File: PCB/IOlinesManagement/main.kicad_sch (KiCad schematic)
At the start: 3 parts

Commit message: Fingerprints assignment
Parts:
- DirControl_1, I/O-LinesToDev_1, I/O-LinesToMicro_1: footprint (none) -> Connector_PinHeader_2.54mm:PinHeader_2x09_P2.54mm_Vertical
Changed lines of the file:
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@@
 			)
 		)
-		(property "Footprint" ""
+		(property "Footprint" "Connector_PinHeader_2.54mm:PinHeader_2x09_P2.54mm_Vertical"
 			(at 222.504 69.088 0)
 			(effects
@@
 			)
 		)
-		(property "Footprint" ""
+		(property "Footprint" "Connector_PinHeader_2.54mm:PinHeader_2x09_P2.54mm_Vertical"
 			(at 139.7 68.834 0)
 			(effects
@@
 			)
 		)
-		(property "Footprint" ""
+		(property "Footprint" "Connector_PinHeader_2.54mm:PinHeader_2x09_P2.54mm_Vertical"
 			(at 52.324 69.85 0)
 			(effects

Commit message: DIRColtrol_1 pins assignment changed
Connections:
- net DIR-1: now also DirControl_1.2 (Pin_2); no longer DirControl_1.1 (Pin_1)
- net DIR-2: now also DirControl_1.4 (Pin_4); no longer DirControl_1.2 (Pin_2)
- net DIR-3: now also DirControl_1.6 (Pin_6); no longer DirControl_1.3 (Pin_3)
- net DIR-4: now also DirControl_1.8 (Pin_8); no longer DirControl_1.4 (Pin_4)
- net DIR-6: now also DirControl_1.1 (Pin_1); no longer DirControl_1.6 (Pin_6)
- net DIR-7: now also DirControl_1.3 (Pin_3); no longer DirControl_1.7 (Pin_7)
- net DIR-8: now also DirControl_1.7 (Pin_7); no longer DirControl_1.8 (Pin_8)

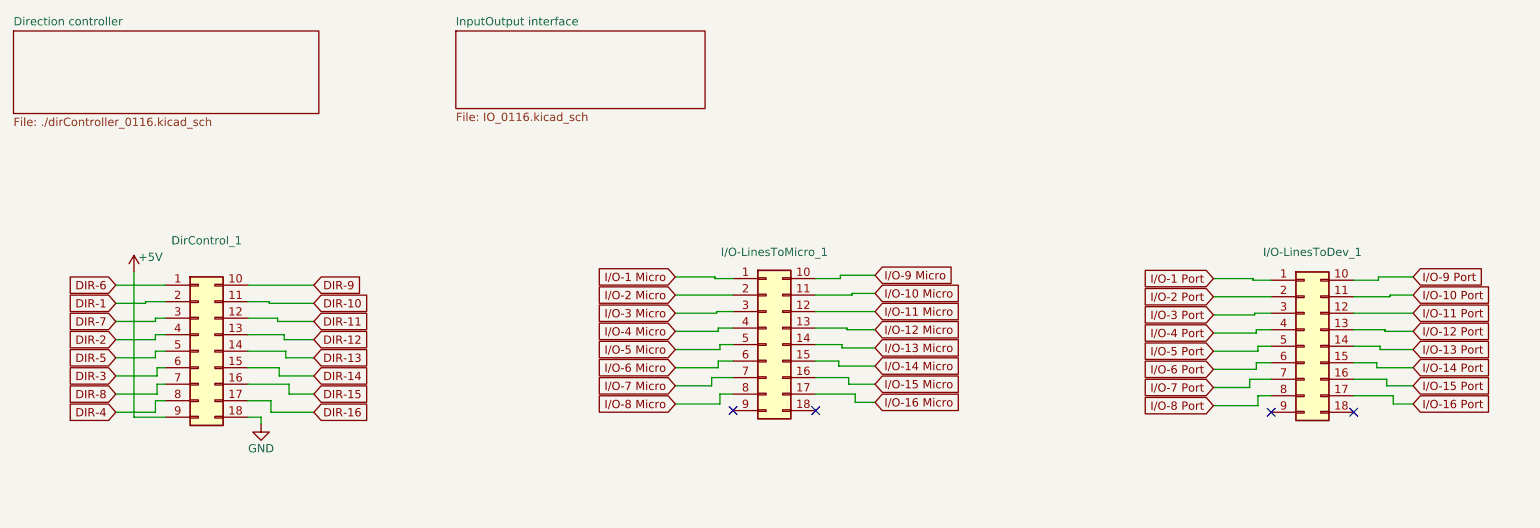
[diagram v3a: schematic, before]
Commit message: Connector pins adjustment
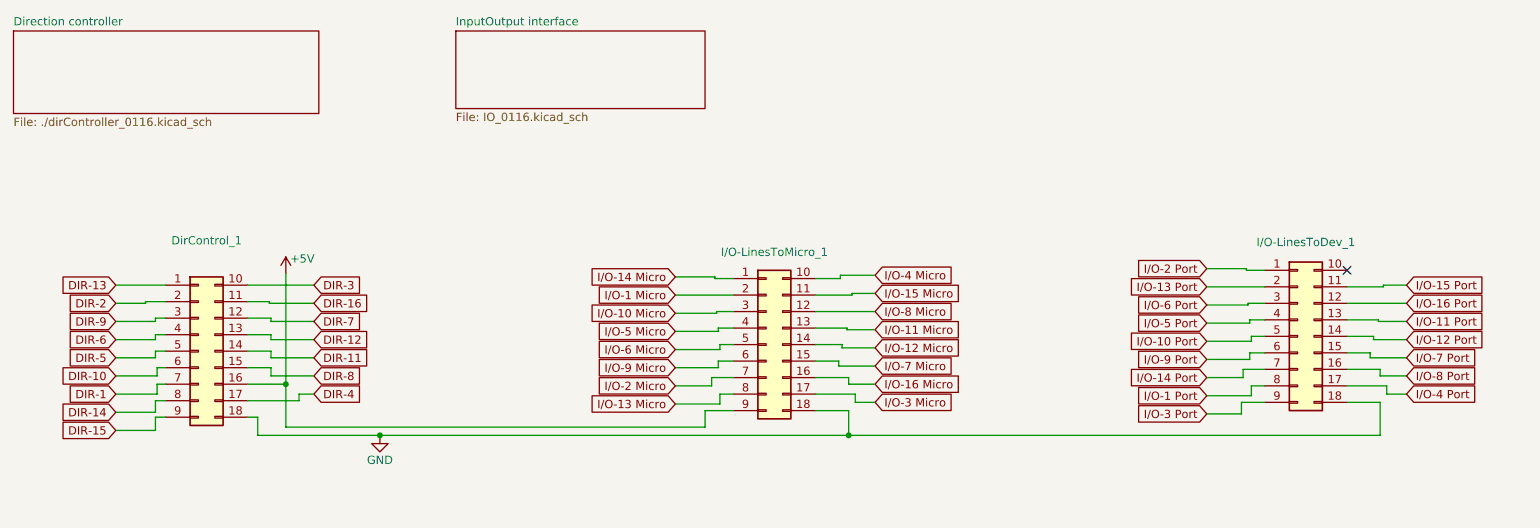
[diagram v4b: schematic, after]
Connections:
- net +5V: now also DirControl_1.16 (Pin_16), I/O-LinesToMicro_1.9 (Pin_9); no longer DirControl_1.9 (Pin_9)
- net DIR-1: now also DirControl_1.7 (Pin_7); no longer DirControl_1.2 (Pin_2)
- net DIR-10: now also DirControl_1.6 (Pin_6); no longer DirControl_1.11 (Pin_11)
- net DIR-11: now also DirControl_1.14 (Pin_14); no longer DirControl_1.12 (Pin_12)
- net DIR-13: now also DirControl_1.1 (Pin_1); no longer DirControl_1.14 (Pin_14)
- net DIR-14: now also DirControl_1.8 (Pin_8); no longer DirControl_1.15 (Pin_15)
- net DIR-15: now also DirControl_1.9 (Pin_9); no longer DirControl_1.16 (Pin_16)
- net DIR-16: now also DirControl_1.11 (Pin_11); no longer DirControl_1.17 (Pin_17)
- net DIR-2: now also DirControl_1.2 (Pin_2); no longer DirControl_1.4 (Pin_4)
- net DIR-3: now also DirControl_1.10 (Pin_10); no longer DirControl_1.6 (Pin_6)
- net DIR-4: now also DirControl_1.17 (Pin_17); no longer DirControl_1.8 (Pin_8)
- net DIR-6: now also DirControl_1.4 (Pin_4); no longer DirControl_1.1 (Pin_1)
- net DIR-7: now also DirControl_1.12 (Pin_12); no longer DirControl_1.3 (Pin_3)
- net DIR-8: now also DirControl_1.15 (Pin_15); no longer DirControl_1.7 (Pin_7)
- net DIR-9: now also DirControl_1.3 (Pin_3); no longer DirControl_1.10 (Pin_10)
- net GND: now also I/O-LinesToDev_1.18 (Pin_18), I/O-LinesToMicro_1.18 (Pin_18)
- net I/O-1 Micro: now also I/O-LinesToMicro_1.2 (Pin_2); no longer I/O-LinesToMicro_1.1 (Pin_1)
- net I/O-1 Port: now also I/O-LinesToDev_1.8 (Pin_8); no longer I/O-LinesToDev_1.1 (Pin_1)
- net I/O-10 Micro: now also I/O-LinesToMicro_1.3 (Pin_3); no longer I/O-LinesToMicro_1.11 (Pin_11)
- net I/O-10 Port: now also I/O-LinesToDev_1.5 (Pin_5); no longer I/O-LinesToDev_1.11 (Pin_11)
- net I/O-11 Micro: now also I/O-LinesToMicro_1.13 (Pin_13); no longer I/O-LinesToMicro_1.12 (Pin_12)
- net I/O-11 Port: now also I/O-LinesToDev_1.13 (Pin_13); no longer I/O-LinesToDev_1.12 (Pin_12)
- net I/O-12 Micro: now also I/O-LinesToMicro_1.14 (Pin_14); no longer I/O-LinesToMicro_1.13 (Pin_13)
- net I/O-12 Port: now also I/O-LinesToDev_1.14 (Pin_14); no longer I/O-LinesToDev_1.13 (Pin_13)
- net I/O-13 Micro: now also I/O-LinesToMicro_1.8 (Pin_8); no longer I/O-LinesToMicro_1.14 (Pin_14)
- net I/O-13 Port: now also I/O-LinesToDev_1.2 (Pin_2); no longer I/O-LinesToDev_1.14 (Pin_14)
- net I/O-14 Micro: now also I/O-LinesToMicro_1.1 (Pin_1); no longer I/O-LinesToMicro_1.15 (Pin_15)
- net I/O-14 Port: now also I/O-LinesToDev_1.7 (Pin_7); no longer I/O-LinesToDev_1.15 (Pin_15)
- net I/O-15 Micro: now also I/O-LinesToMicro_1.11 (Pin_11); no longer I/O-LinesToMicro_1.16 (Pin_16)
- net I/O-15 Port: now also I/O-LinesToDev_1.11 (Pin_11); no longer I/O-LinesToDev_1.16 (Pin_16)
- net I/O-16 Micro: now also I/O-LinesToMicro_1.16 (Pin_16); no longer I/O-LinesToMicro_1.17 (Pin_17)
- net I/O-16 Port: now also I/O-LinesToDev_1.12 (Pin_12); no longer I/O-LinesToDev_1.17 (Pin_17)
- net I/O-2 Micro: now also I/O-LinesToMicro_1.7 (Pin_7); no longer I/O-LinesToMicro_1.2 (Pin_2)
- net I/O-2 Port: now also I/O-LinesToDev_1.1 (Pin_1); no longer I/O-LinesToDev_1.2 (Pin_2)
- net I/O-3 Micro: now also I/O-LinesToMicro_1.17 (Pin_17); no longer I/O-LinesToMicro_1.3 (Pin_3)
- net I/O-3 Port: now also I/O-LinesToDev_1.9 (Pin_9); no longer I/O-LinesToDev_1.3 (Pin_3)
- net I/O-4 Micro: now also I/O-LinesToMicro_1.10 (Pin_10); no longer I/O-LinesToMicro_1.4 (Pin_4)
- net I/O-4 Port: now also I/O-LinesToDev_1.17 (Pin_17); no longer I/O-LinesToDev_1.4 (Pin_4)
- net I/O-5 Micro: now also I/O-LinesToMicro_1.4 (Pin_4); no longer I/O-LinesToMicro_1.5 (Pin_5)
- net I/O-5 Port: now also I/O-LinesToDev_1.4 (Pin_4); no longer I/O-LinesToDev_1.5 (Pin_5)
- net I/O-6 Micro: now also I/O-LinesToMicro_1.5 (Pin_5); no longer I/O-LinesToMicro_1.6 (Pin_6)
- net I/O-6 Port: now also I/O-LinesToDev_1.3 (Pin_3); no longer I/O-LinesToDev_1.6 (Pin_6)
- net I/O-7 Micro: now also I/O-LinesToMicro_1.15 (Pin_15); no longer I/O-LinesToMicro_1.7 (Pin_7)
- net I/O-7 Port: now also I/O-LinesToDev_1.15 (Pin_15); no longer I/O-LinesToDev_1.7 (Pin_7)
- net I/O-8 Micro: now also I/O-LinesToMicro_1.12 (Pin_12); no longer I/O-LinesToMicro_1.8 (Pin_8)
- net I/O-8 Port: now also I/O-LinesToDev_1.16 (Pin_16); no longer I/O-LinesToDev_1.8 (Pin_8)
- net I/O-9 Micro: now also I/O-LinesToMicro_1.6 (Pin_6); no longer I/O-LinesToMicro_1.10 (Pin_10)
- net I/O-9 Port: now also I/O-LinesToDev_1.6 (Pin_6); no longer I/O-LinesToDev_1.10 (Pin_10)
- no-connect marks 4 -> 1
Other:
- moved on the sheet: I/O-LinesToDev_1

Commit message: Fixes and updates
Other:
- sheet InputOutput interface renamed InputLines interface
- added sheet OutputLines Interface (outputs_0116.kicad_sch)
- sheet InputLines interface: file IO_0116.kicad_sch -> inputs_0116.kicad_sch
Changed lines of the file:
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@@
+	)
+	(sheet
+		(at 145.796 20.574)
+		(size 40.386 11.938)
+		(exclude_from_sim no)
+		(in_bom yes)
+		(on_board yes)
+		(dnp no)
+		(fields_autoplaced yes)
+		(stroke
+			(width 0.1524)
+			(type solid)
+		)
+		(fill
+			(color 0 0 0 0.0000)
+		)
+		(property "Sheetname" "OutputLines Interface"
+			(at 145.796 19.8624 0)
+			(effects
+				(font
+					(size 1.27 1.27)
+				)
+				(justify left bottom)
+			)
+		)
+		(property "Sheetfile" "outputs_0116.kicad_sch"
+			(at 145.796 33.0966 0)
+			(effects
+				(font
+					(size 1.27 1.27)
+				)
+				(justify left top)
+			)
+		)
+		(instances
+			(project "main"
+				(path "/e1cfbeff-02ed-44cc-ae25-dce7e255cb28"
+					(page "4")
+				)
+			)
+		)
 	)
 	(sheet
@@
 			(color 0 0 0 0.0000)
 		)
-		(property "Sheetname" "InputOutput interface"
+		(property "Sheetname" "InputLines interface"
 			(at 91.948 19.8624 0)
 			(effects
@@
 			)
 		)
-		(property "Sheetfile" "IO_0116.kicad_sch"
+		(property "Sheetfile" "inputs_0116.kicad_sch"
 			(at 91.948 33.0966 0)
 			(effects

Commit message: Fixes...
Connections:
- net +5V: now also I/O-LinesToDev_1.10 (Pin_10)
- no-connect marks 1 -> 0
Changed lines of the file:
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@@
+	)
+	(junction
+		(at 94.996 81.534)
+		(diameter 0)
+		(color 0 0 0 0)
 	)
 	(junction
@@
 		(color 0 0 0 0)
 	)
-	(no_connect
-		(at 229.108 57.404)
-	)
 	(wire
 		(pts
@@
 	(wire
 		(pts
+			(xy 94.996 81.534) (xy 94.996 47.752)
+		)
+		(stroke
+			(width 0)
+			(type default)
+		)
+	)
+	(wire
+		(pts
 			(xy 216.408 65.024) (xy 214.122 65.024)
 		)
@@
 	(wire
 		(pts
+			(xy 234.696 47.752) (xy 234.696 57.404)
+		)
+		(stroke
+			(width 0)
+			(type default)
+		)
+	)
+	(wire
+		(pts
 			(xy 63.246 62.484) (xy 63.246 62.23)
 		)
@@
 	(wire
 		(pts
+			(xy 94.996 81.534) (xy 130.302 81.534)
+		)
+		(stroke
+			(width 0)
+			(type default)
+		)
+	)
+	(wire
+		(pts
 			(xy 156.464 69.342) (xy 151.384 69.342)
 		)
@@
 	(wire
 		(pts
+			(xy 234.696 57.404) (xy 229.108 57.404)
+		)
+		(stroke
+			(width 0)
+			(type default)
+		)
+	)
+	(wire
+		(pts
 			(xy 59.944 69.85) (xy 63.5 69.85)
 		)
@@
 	(wire
 		(pts
-			(xy 65.786 81.534) (xy 130.302 81.534)
+			(xy 65.786 81.534) (xy 94.996 81.534)
 		)
 		(stroke
@@
 		)
 		(stroke
+			(width 0)
+			(type default)
+		)
+	)
+	(wire
+		(pts
+			(xy 94.996 47.752) (xy 234.696 47.752)
+		)
+		(stroke

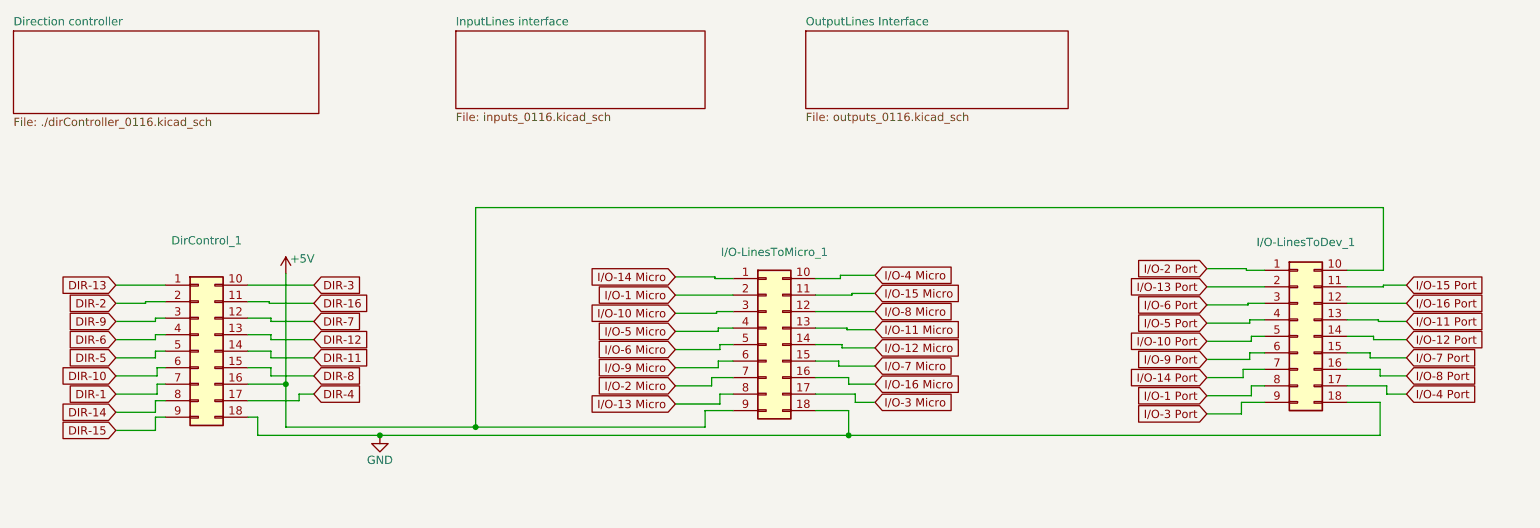
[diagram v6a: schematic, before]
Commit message: Connectors pins-map has been changed
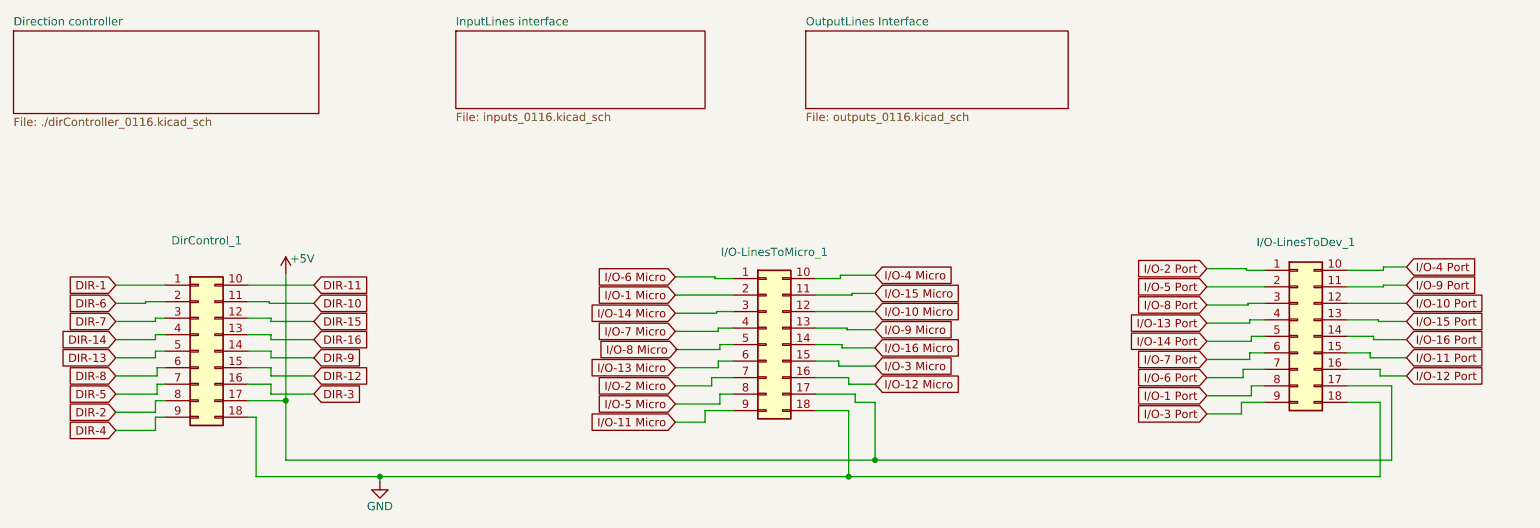
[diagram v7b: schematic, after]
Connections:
- net +5V: now also DirControl_1.17 (Pin_17), I/O-LinesToDev_1.17 (Pin_17), I/O-LinesToMicro_1.17 (Pin_17); no longer DirControl_1.16 (Pin_16), I/O-LinesToDev_1.10 (Pin_10), I/O-LinesToMicro_1.9 (Pin_9)
- net DIR-1: now also DirControl_1.1 (Pin_1); no longer DirControl_1.7 (Pin_7)
- net DIR-10: now also DirControl_1.11 (Pin_11); no longer DirControl_1.6 (Pin_6)
- net DIR-11: now also DirControl_1.10 (Pin_10); no longer DirControl_1.14 (Pin_14)
- net DIR-12: now also DirControl_1.15 (Pin_15); no longer DirControl_1.13 (Pin_13)
- net DIR-13: now also DirControl_1.5 (Pin_5); no longer DirControl_1.1 (Pin_1)
- net DIR-14: now also DirControl_1.4 (Pin_4); no longer DirControl_1.8 (Pin_8)
- net DIR-15: now also DirControl_1.12 (Pin_12); no longer DirControl_1.9 (Pin_9)
- net DIR-16: now also DirControl_1.13 (Pin_13); no longer DirControl_1.11 (Pin_11)
- net DIR-2: now also DirControl_1.8 (Pin_8); no longer DirControl_1.2 (Pin_2)
- net DIR-3: now also DirControl_1.16 (Pin_16); no longer DirControl_1.10 (Pin_10)
- net DIR-4: now also DirControl_1.9 (Pin_9); no longer DirControl_1.17 (Pin_17)
- net DIR-5: now also DirControl_1.7 (Pin_7); no longer DirControl_1.5 (Pin_5)
- net DIR-6: now also DirControl_1.2 (Pin_2); no longer DirControl_1.4 (Pin_4)
- net DIR-7: now also DirControl_1.3 (Pin_3); no longer DirControl_1.12 (Pin_12)
- net DIR-8: now also DirControl_1.6 (Pin_6); no longer DirControl_1.15 (Pin_15)
- net DIR-9: now also DirControl_1.14 (Pin_14); no longer DirControl_1.3 (Pin_3)
- net I/O-10 Micro: now also I/O-LinesToMicro_1.12 (Pin_12); no longer I/O-LinesToMicro_1.3 (Pin_3)
- net I/O-10 Port: now also I/O-LinesToDev_1.12 (Pin_12); no longer I/O-LinesToDev_1.5 (Pin_5)
- net I/O-11 Micro: now also I/O-LinesToMicro_1.9 (Pin_9); no longer I/O-LinesToMicro_1.13 (Pin_13)
- net I/O-11 Port: now also I/O-LinesToDev_1.15 (Pin_15); no longer I/O-LinesToDev_1.13 (Pin_13)
- net I/O-12 Micro: now also I/O-LinesToMicro_1.16 (Pin_16); no longer I/O-LinesToMicro_1.14 (Pin_14)
- net I/O-12 Port: now also I/O-LinesToDev_1.16 (Pin_16); no longer I/O-LinesToDev_1.14 (Pin_14)
- net I/O-13 Micro: now also I/O-LinesToMicro_1.6 (Pin_6); no longer I/O-LinesToMicro_1.8 (Pin_8)
- net I/O-13 Port: now also I/O-LinesToDev_1.4 (Pin_4); no longer I/O-LinesToDev_1.2 (Pin_2)
- net I/O-14 Micro: now also I/O-LinesToMicro_1.3 (Pin_3); no longer I/O-LinesToMicro_1.1 (Pin_1)
- net I/O-14 Port: now also I/O-LinesToDev_1.5 (Pin_5); no longer I/O-LinesToDev_1.7 (Pin_7)
- net I/O-15 Port: now also I/O-LinesToDev_1.13 (Pin_13); no longer I/O-LinesToDev_1.11 (Pin_11)
- net I/O-16 Micro: now also I/O-LinesToMicro_1.14 (Pin_14); no longer I/O-LinesToMicro_1.16 (Pin_16)
- net I/O-16 Port: now also I/O-LinesToDev_1.14 (Pin_14); no longer I/O-LinesToDev_1.12 (Pin_12)
- net I/O-3 Micro: now also I/O-LinesToMicro_1.15 (Pin_15); no longer I/O-LinesToMicro_1.17 (Pin_17)
- net I/O-4 Port: now also I/O-LinesToDev_1.10 (Pin_10); no longer I/O-LinesToDev_1.17 (Pin_17)
- net I/O-5 Micro: now also I/O-LinesToMicro_1.8 (Pin_8); no longer I/O-LinesToMicro_1.4 (Pin_4)
- net I/O-5 Port: now also I/O-LinesToDev_1.2 (Pin_2); no longer I/O-LinesToDev_1.4 (Pin_4)
- net I/O-6 Micro: now also I/O-LinesToMicro_1.1 (Pin_1); no longer I/O-LinesToMicro_1.5 (Pin_5)
- net I/O-6 Port: now also I/O-LinesToDev_1.7 (Pin_7); no longer I/O-LinesToDev_1.3 (Pin_3)
- net I/O-7 Micro: now also I/O-LinesToMicro_1.4 (Pin_4); no longer I/O-LinesToMicro_1.15 (Pin_15)
- net I/O-7 Port: now also I/O-LinesToDev_1.6 (Pin_6); no longer I/O-LinesToDev_1.15 (Pin_15)
- net I/O-8 Micro: now also I/O-LinesToMicro_1.5 (Pin_5); no longer I/O-LinesToMicro_1.12 (Pin_12)
- net I/O-8 Port: now also I/O-LinesToDev_1.3 (Pin_3); no longer I/O-LinesToDev_1.16 (Pin_16)
- net I/O-9 Micro: now also I/O-LinesToMicro_1.13 (Pin_13); no longer I/O-LinesToMicro_1.6 (Pin_6)
- net I/O-9 Port: now also I/O-LinesToDev_1.11 (Pin_11); no longer I/O-LinesToDev_1.6 (Pin_6)
